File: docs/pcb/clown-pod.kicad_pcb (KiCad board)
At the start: 2 copper layers, 70 x 30 mm, 21 parts, among them J1 Cell, PH2.0, J2 Strip SM-3, J3 Elbow SM-4, Q1 RFP30N06LE, SW1 KCD1 rocker, U1 MT3608 module, U2 74AHCT125, U3 XIAO ESP32-C3

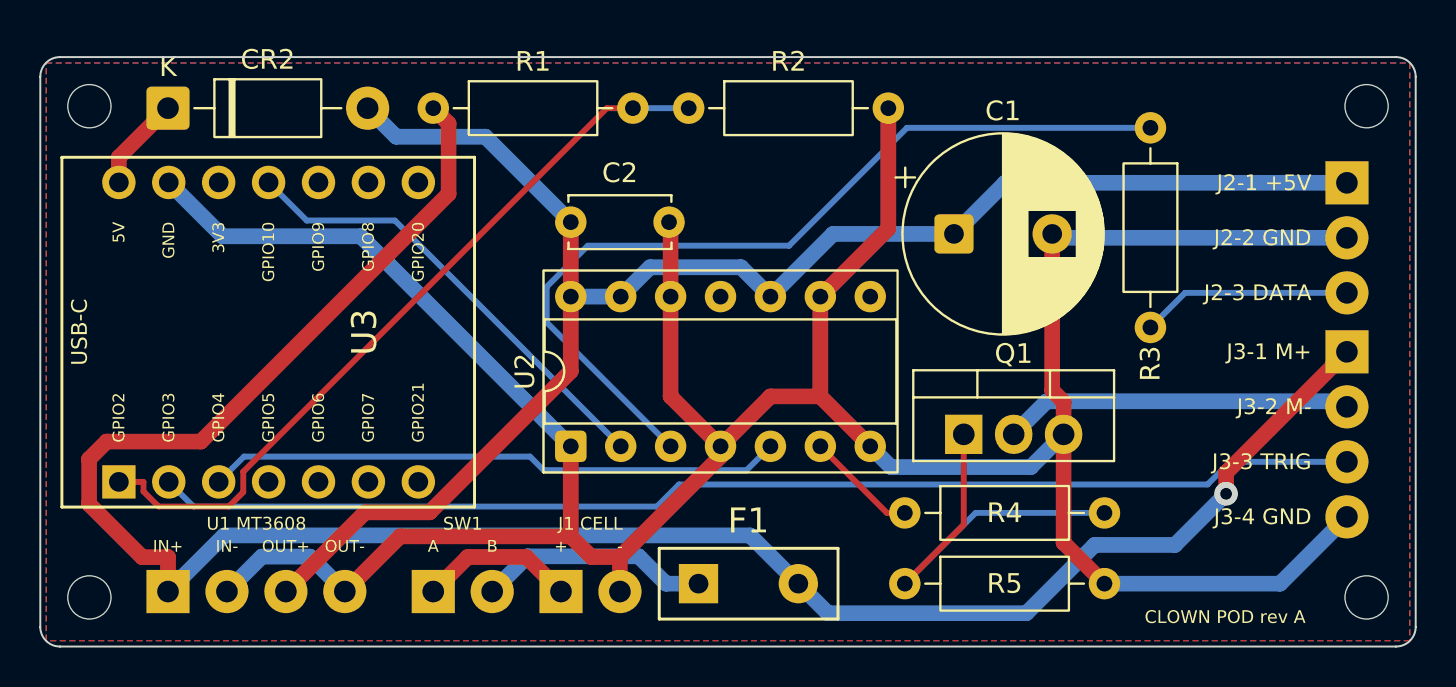
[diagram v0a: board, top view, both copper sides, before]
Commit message: Re-lay out the pod PCB after review: hand-routed power, poured ground
Fixes from four review agents and two re-reviews:
- Power stage moved beside J3; cell, switch, fuse and motor paths
  hand-routed at 1.5 mm, +5V trunk U1 -> C1 -> J2 clear of U2's pins
- GND is pours plus 55 stitching vias, no routed ground
- 0.4 mm clearance everywhere, no copper within 2.4 mm of a hole
- R6 and C3 added; Q1 moved clear of U2's body
- Silkscreen at least 0.8 mm / 0.15 mm, nothing off the edge; DRC now
  fails on silk problems; pour 0.5 mm from the edge
- XIAO moved 1.5 mm left so its USB-C stands proud of the edge
- README gives the PCBWay form settings that differ from the defaults

DRC with all severities: no errors, one starved-thermal warning on a pad
that also joins the back pour.

Co-Authored-By: Claude Opus 5.5 <noreply@anthropic.com>
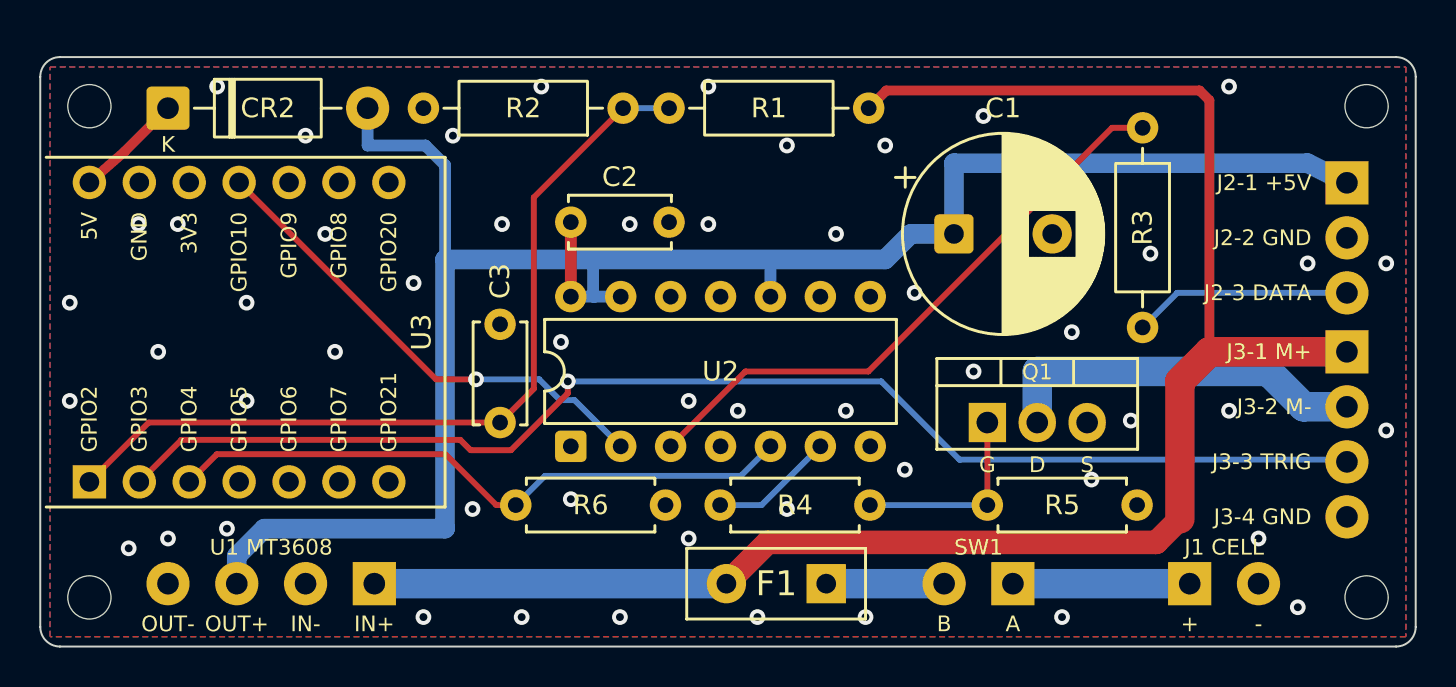
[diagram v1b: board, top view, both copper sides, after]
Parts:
- added C3: 0.1uF, C_Disc_D5.0mm_W2.5mm_P5.00mm, F.Cu at (23.4, 18.6)
- added R6: 100k, R_Axial_DIN0207_L6.3mm_D2.5mm_P7.62mm_Horizontal, F.Cu at (24.2, 22.8)
- J1: footprint clown:J1 -> clown:WirePads_2
- J2: footprint clown:J2 -> clown:WirePads_3
- J3: footprint clown:J3 -> clown:WirePads_4
- R4, R5: footprint R_Axial_DIN0207_L6.3mm_D2.5mm_P10.16mm_Horizontal -> R_Axial_DIN0207_L6.3mm_D2.5mm_P7.62mm_Horizontal
- SW1: footprint clown:SW1 -> clown:WirePads_2
- U1: footprint clown:U1 -> clown:WirePads_4
- U2: footprint DIP-14_W7.62mm_Socket -> DIP-14_W7.62mm
- moved J1 32.0 mm to (58.5, 26.8)
- moved SW1 29.5 mm to (49.5, 26.8)
- moved R1 22.2 mm to (42.2, 2.60), turned to 180 degrees
- moved U1 10.5 mm to (17.0, 26.8)
- moved R4 9.41 mm to (34.6, 22.8)
- moved F1 6.50 mm to (40.0, 26.8)
- moved R5 5.80 mm to (48.2, 22.8)
- moved R2 3.34 mm to (29.7, 2.60), turned to 180 degrees
- moved U3 1.50 mm to (2.50, 21.6)
- moved Q1 1.34 mm to (48.2, 18.6)
- moved R3 0.40 mm to (56.1, 3.60)
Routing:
- net GND: track 160.2 -> 0.00 mm, vias 0 -> 55
- net VBATT: track 106.7 -> 89.2 mm, vias 1 -> 0
- net +5V: track 82.6 -> 97.7 mm
- net LED_DATA: track 44.8 -> 30.7 mm
- net GATE_Q: track 20.5 -> 10.2 mm
- net VBATT_SW: track 11.8 -> 6.00 mm
- net TRIG: track 61.4 -> 66.1 mm, vias 0 -> 1
- net VSENSE: track 38.8 -> 43.1 mm
- net GATE_3V3: track 29.4 -> 32.5 mm
- net LED_DATA_3V3: track 23.5 -> 25.0 mm, vias 0 -> 1
- net MOTOR-: track 17.8 -> 19.1 mm
- net VBATT_RAW: track 7.95 -> 9.00 mm
- net +5V_MCU: track 4.82 -> 5.51 mm
- net GATE: track 5.70 -> 6.34 mm
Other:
- board text added: "D"
- board text added: "G"
- board text added: "S"
- board text added: "Trim U1 to 5.00 V"
- board text added: "before fitting U3"
- board text removed: "Trim U1 to 5.00 V before fitting U3"
- board text removed: "USB-C"

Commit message: Fit F1's real 15 mm polyfuse disc on the pod PCB
The GBX part measures 15 mm across on 5 mm-pitch legs, standing on kinks
3 mm off the board. The 9 mm outline it had would have run into SW1.
F1 moves left into the bottom-row gap between U1 and SW1, and the
VBATT/VBATT_SW tracks move with it. C1 measures 10 mm, as the footprint
assumed. DRC: no errors, no unconnected pads.

Co-Authored-By: Claude Opus 5.5 <noreply@anthropic.com>
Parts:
- F1: footprint clown:PPTC_Radial_P5.08mm -> clown:PPTC_Disc_D15mm_P5.08mm
- moved F1 5.96 mm to (34.0, 26.8)
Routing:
- net VBATT_SW: track 6.00 -> 12.0 mm
- net LED_DATA: track 30.7 -> 35.1 mm, vias 0 -> 1
- net VSENSE: track 43.1 -> 45.6 mm, vias 0 -> 1
- net LED_DATA_3V3: track 25.0 -> 27.1 mm, vias 1 -> 0
- net TRIG: track 66.1 -> 67.3 mm
- net +5V: track 97.7 -> 98.5 mm
- net GND: vias 55 -> 60
